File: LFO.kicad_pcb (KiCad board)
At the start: 2 copper layers, 39.6 x 100 mm, 98 parts, among them J1 AudioJack2_SwitchT, J2 AudioJack2_SwitchT, J3 AudioJack2_SwitchT, J4 AudioJack2_SwitchT, J5 AudioJack2_SwitchT, J6 AudioJack2_SwitchT, J7 Conn_02x03_Odd_Even, J8 Conn_02x05_Odd_Even, Q1 BC847, SW1 SW_Push, SW2 SW_SPDT_MSM, SW3 SW_SPDT_MSM, U1 ATtiny84-20MU, U2 74AHCT1G125, U3 MCP6002-xMS, U4 MCP6002-xMS, U5 L7805, U6 LM324, Y1 20MHz

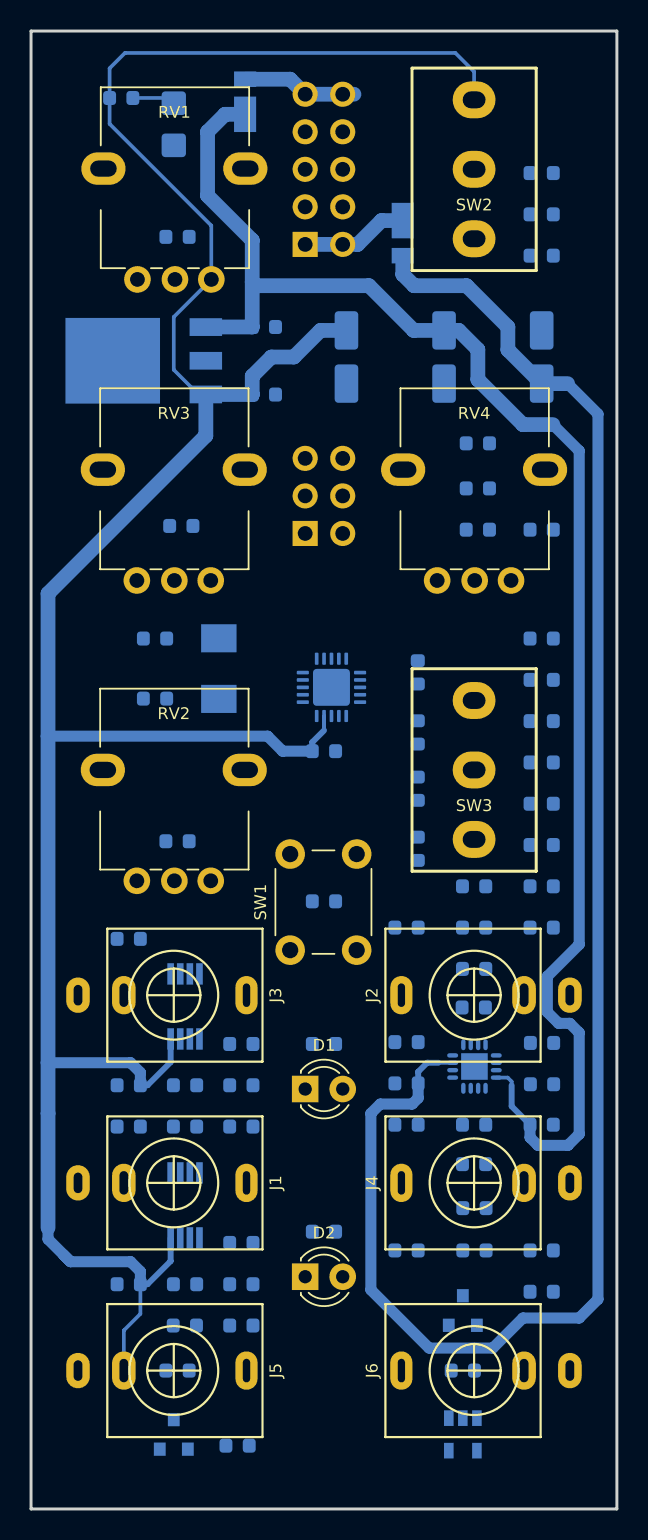
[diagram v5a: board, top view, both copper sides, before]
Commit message: Autorouted signals and manual pours and adjustments.
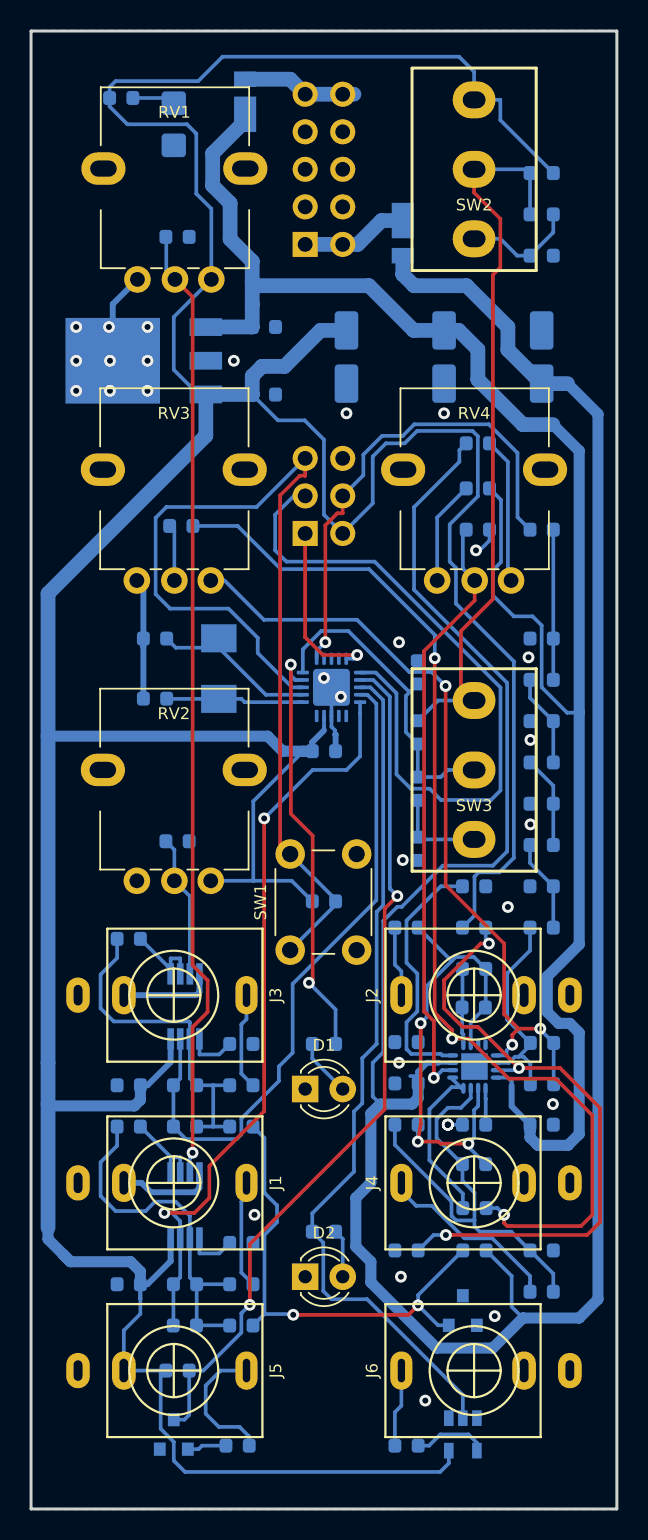
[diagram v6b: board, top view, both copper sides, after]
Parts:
- moved R5 6.35 mm to (154.1, 150.7)
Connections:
- C1 pad 1: (no net) -> GND
- C10 pad 2: (no net) -> GND
- C11 pad 2: (no net) -> GND
- C12 pad 2: (no net) -> GND
- C13 pad 2: (no net) -> GND
- C14 pad 1: (no net) -> GND
- C17 pad 2: (no net) -> GND
- C18 pad 2: (no net) -> GND
- C19 pad 2: (no net) -> GND
- C2 pad 1: (no net) -> GND
- C20 pad 2: (no net) -> GND
- C22 pad 2: (no net) -> GND
- C23 pad 2: (no net) -> GND
- C24 pad 1: (no net) -> GND
- C25 pad 2: (no net) -> GND
- C3 pad 2: (no net) -> GND
- C5 pad 2: (no net) -> GND
- C6 pad 2: (no net) -> GND
- C8 pad 2: (no net) -> GND
- C9 pad 2: (no net) -> GND
- D1 pad 1: (no net) -> GND
- D2 pad 1: (no net) -> GND
- D4 pad 1: (no net) -> GND
- D6 pad 1: (no net) -> GND
- J1 pad S: (no net) -> GND
- J1 pad TN: (no net) -> GND
- J2 pad S: (no net) -> GND
- J3 pad S: (no net) -> GND
- J3 pad TN: (no net) -> GND
- J4 pad S: (no net) -> GND
- J5 pad S: (no net) -> GND
- J6 pad S: (no net) -> GND
- J7 pad 6: (no net) -> GND
- J8 pad 3: (no net) -> GND
- J8 pad 4: (no net) -> GND
- J8 pad 5: (no net) -> GND
- J8 pad 6: (no net) -> GND
- J8 pad 7: (no net) -> GND
- J8 pad 8: (no net) -> GND
- Q1 pad 2: (no net) -> GND
- R11 pad 2: (no net) -> GND
- R16 pad 2: (no net) -> GND
- R27 pad 2: (no net) -> GND
- R28 pad 1: (no net) -> GND
- R30 pad 1: (no net) -> GND
- R35 pad 2: (no net) -> GND
- R36 pad 1: (no net) -> GND
- R42 pad 2: (no net) -> GND
- R43 pad 2: (no net) -> GND
- RV1 pad 3: (no net) -> GND
- RV2 pad 3: (no net) -> GND
- RV3 pad 3: (no net) -> GND
- SW1 pad 2: (no net) -> GND
- U1 pad 21: (no net) -> GND
- U1 pad 8: (no net) -> GND
- U2 pad 1: (no net) -> GND
- U2 pad 3: (no net) -> GND
- U3 pad 4: (no net) -> GND
- U4 pad 4: (no net) -> GND
- U5 pad 2: (no net) -> GND
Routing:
- net +5V: track 181.5 -> 303.7 mm
- net Net-(C16-Pad2): track 0.00 -> 79.9 mm, vias 0 -> 3
- net RESET: track 0.00 -> 67.1 mm
- net Net-(C5-Pad1): track 0.00 -> 65.0 mm, vias 0 -> 1
- net -12V: track 117.5 -> 179.3 mm
- net SYNC: track 0.00 -> 58.9 mm, vias 0 -> 2
- net TRIG: track 0.00 -> 58.1 mm
- net Net-(C15-Pad1): track 0.00 -> 52.5 mm, vias 0 -> 3
- net FREQ: track 0.00 -> 51.1 mm, vias 0 -> 2
- net Net-(R38-Pad2): track 0.00 -> 49.2 mm
- net SCK: track 0.00 -> 47.6 mm
- net PWM: track 0.00 -> 45.5 mm
- net Net-(R29-Pad1): track 0.00 -> 43.3 mm, vias 0 -> 3
- net Net-(C22-Pad1): track 0.00 -> 40.7 mm, vias 0 -> 1
- net Net-(C16-Pad1): track 0.00 -> 36.5 mm, vias 0 -> 3
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- added copper zone on B.Cu, net GND
- added copper zone on F.Cu, net GND
